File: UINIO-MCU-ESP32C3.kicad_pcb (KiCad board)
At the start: 2 copper layers, 60.3 x 20.4 mm, 50 parts, among them J1 Conn_01x15_Male, J2 外接串行下载接口, J3 Conn_01x15_Male, SW1 复位按键, SW2 下载按键, U1 ME6211C33M5G-N, U2 W25Q128JVSSIQ, U3 ESP32-C3, U4 CH343P, Y1 40MHz

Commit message: Complete wiring.
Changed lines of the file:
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@@
   (segment (start 134.37 111.72) (end 138.18 111.72) (width 0.5) (layer "B.Cu") (net 4))
   (segment (start 129.62 100.52) (end 129.62 106.97) (width 0.5) (layer "B.Cu") (net 4))
-  (segment (start 167.73 101.035903) (end 167.73 99.95) (width 0.2) (layer "F.Cu") (net 5))
   (segment (start 170.155 98.43) (end 169.25 98.43) (width 0.2) (layer "F.Cu") (net 5))
+  (segment (start 168.083553 99.596446) (end 169.25 98.43) (width 0.2) (layer "F.Cu") (net 5))
+  (segment (start 167.73 100.45) (end 167.73 101.035903) (width 0.2) (layer "F.Cu") (net 5))
   (segment (start 166.300677 102.465226) (end 167.73 101.035903) (width 0.2) (layer "F.Cu") (net 5))
-  (segment (start 167.73 99.95) (end 169.25 98.43) (width 0.2) (layer "F.Cu") (net 5))
+  (arc (start 167.73 100.45) (mid 167.821884 99.988059) (end 168.083552 99.596445) (width 0.2) (layer "F.Cu") (net 5))
   (segment (start 164.43 98.45) (end 164.43 100.093263) (width 0.2) (layer "F.Cu") (net 6))
   (segment (start 153.185 104.575) (end 150.51 104.575) (width 0.2) (layer "F.Cu") (net 6))
@@
   (via (at 131.62 96.7605) (size 0.5) (drill 0.2) (layers "F.Cu" "B.Cu") (net 23))
   (via (at 131.63 101.73) (size 0.5) (drill 0.2) (layers "F.Cu" "B.Cu") (net 23))
+  (segment (start 165.095185 105.824815) (end 164.94 105.98) (width 0.2) (layer "B.Cu") (net 23))
+  (segment (start 131.63 97.6695) (end 131.62 97.6595) (width 0.2) (layer "B.Cu") (net 23))
+  (segment (start 161.82 105.98) (end 152.61 96.77) (width 0.2) (layer "B.Cu") (net 23))
+  (segment (start 164.94 105.98) (end 161.82 105.98) (width 0.2) (layer "B.Cu") (net 23))
+  (segment (start 131.62 96.77) (end 130.57 95.72) (width 0.2) (layer "B.Cu") (net 23))
   (segment (start 130.57 95.72) (end 130.57 94.15) (width 0.2) (layer "B.Cu") (net 23))
-  (segment (start 131.63 97.6695) (end 131.62 97.6595) (width 0.2) (layer "B.Cu") (net 23))
-  (segment (start 161.664815 105.824815) (end 152.61 96.77) (width 0.2) (layer "B.Cu") (net 23))
   (segment (start 131.63 101.73) (end 131.63 97.6695) (width 0.2) (layer "B.Cu") (net 23))
   (segment (start 152.61 96.77) (end 131.62 96.77) (width 0.2) (layer "B.Cu") (net 23))
-  (segment (start 131.62 96.77) (end 130.57 95.72) (width 0.2) (layer "B.Cu") (net 23))
-  (segment (start 165.095185 105.824815) (end 161.664815 105.824815) (width 0.2) (layer "B.Cu") (net 23))
   (segment (start 130.96 101.13) (end 134.259 101.13) (width 0.2) (layer "F.Cu") (net 24))
   (segment (start 165.804447 105.755553) (end 165.73303 105.755553) (width 0.2) (layer "F.Cu") (net 24))

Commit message: Ready for release.
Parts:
- AE1: value Antenna -> Antenna_Dipole
- moved C7 13.2 mm to (167.4, 98.5), turned to 90 degrees
- moved C5 12.9 mm to (166.5, 98.5), turned to 90 degrees
- moved C4 12.7 mm to (165.5, 98.5), turned to 90 degrees
- moved C19 2.41 mm to (156.5, 104.9)
- moved C18 1.63 mm to (156.4, 103.2)
- moved C8 1.53 mm to (169.0, 100.4), turned to -45 degrees
- moved C14 1.36 mm to (156.4, 98.6)
- moved R4 1.35 mm to (156.4, 99.7)
- moved C10 1.29 mm to (169.2, 102.8)
- moved L1 1.19 mm to (169.7, 99.1), turned to -135 degrees
- moved C6 1.14 mm to (171.0, 98.5), turned to -45 degrees
- moved C12 0.99 mm to (169.2, 103.7)
- moved R2 0.66 mm to (161.2, 98.5)
- moved AE1 0.46 mm to (175.5, 98.4)
- moved HOLE4 0.41 mm to (176.1, 111.7)
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- renumbered HOLE** to HOLE1, HOLE** to HOLE2, HOLE** to HOLE3, HOLE** to HOLE4, HOLE** to HOLE5
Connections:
- AE1 pad 1: Net-(AE1-Pad1) -> GND
- AE1 pad 2: (no net) -> Net-(AE1-Pad2)
- C6 pad 1: Net-(AE1-Pad1) -> Net-(AE1-Pad2)
- L1 pad 1: Net-(AE1-Pad1) -> Net-(AE1-Pad2)
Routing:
- net GND: track 143.0 -> 185.3 mm, vias 27 -> 24
- net Net-(AE1-Pad2): track 0.00 -> 6.24 mm
- net Net-(AE1-Pad1): track 4.82 -> 0.00 mm
- net /VDD_3.3V: track 132.1 -> 134.8 mm
- net Net-(C8-Pad1): track 6.10 -> 4.27 mm
- net /CHIP_EN: track 32.7 -> 31.9 mm
- net /GPIO5/ADC2/SCL: track 8.25 -> 9.00 mm
- net /VDD_SPI/GPIO11: track 22.7 -> 22.2 mm
- net /GPIO1/U1RXD: vias 0 -> 1
- net /GPIO0/U1TXD: vias 0 -> 1
- net /GPIO2: vias 0 -> 1
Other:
- board size 60.3 x 20.4 mm -> 59.8 x 20.4 mm
- board text added: "ADC2 IO5 SCL"
- board text added: "CHIP_EN"
- board text added: "IO0 TXD1"
- board text added: "IO1 RXD1"
- board text added: "IO11 VDD_SPI"
- board text added: "IO12 SPIHD"
- board text added: "IO13 SPIWP"
- board text added: "IO18 USB_D-"
- board text added: "IO19 USB_D+"
- board text added: "IO8"
- board text added: "IO8 PWM"
- board text added: "IO9 BOOT"

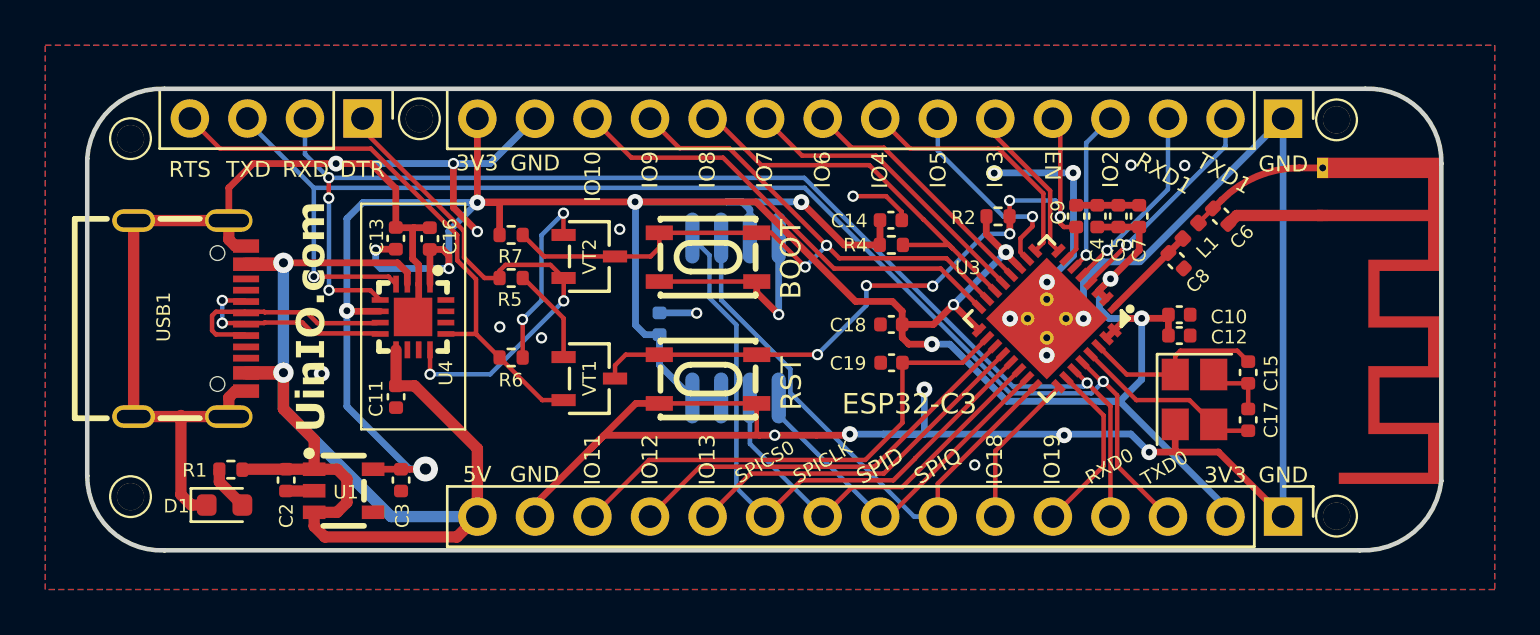
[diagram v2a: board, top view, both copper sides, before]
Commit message: Release UINIO-MCU-ESP32C3 version 1.0.0.
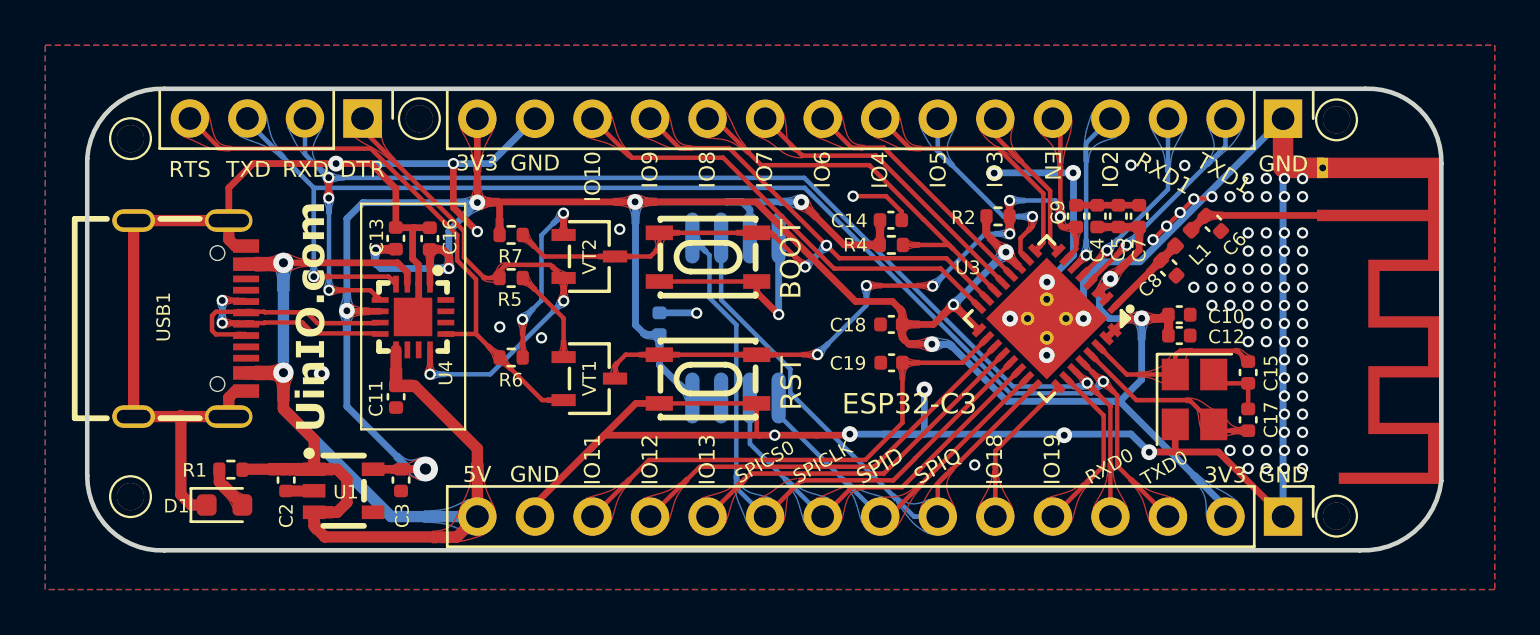
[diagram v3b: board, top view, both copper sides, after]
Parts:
- AE1: value Antenna_Dipole -> Antenna_Chip
- moved ? 1.36 mm to (164.3, 102.9)
- moved C6 0.46 mm to (170.7, 98.8)
- moved C8 0.46 mm to (168.7, 100.7)
- moved L1 0.46 mm to (169.3, 99.4)
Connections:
- AE1 pad 1: GND -> Net-(AE1-Pad1)
- AE1 pad 2: Net-(AE1-Pad2) -> GND
- C6 pad 1: Net-(AE1-Pad2) -> Net-(AE1-Pad1)
- L1 pad 1: Net-(AE1-Pad2) -> Net-(AE1-Pad1)
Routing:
- net Net-(AE1-Pad2): track 6.24 -> 0.00 mm
- net Net-(AE1-Pad1): track 0.00 -> 6.08 mm
- net GND: track 185.3 -> 190.0 mm, vias 24 -> 92
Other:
- board text added: "ADC1 IO4 SDA"

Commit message: Release UINIO-MCU-ESP32C3 version 1.0.0.
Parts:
- moved ? 0.49 mm to (164.8, 102.9)
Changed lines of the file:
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@@
   )
   (footprint "LOGO" (layer "B.Cu")
-    (at 164.311731 102.941526 180)
+    (at 164.8 102.941526 180)
     (attr board_only exclude_from_pos_files exclude_from_bom)
     (fp_text reference "" (at 0 0) (layer "B.SilkS")

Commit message: update
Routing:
- net GND: track 190.0 -> 210.5 mm, vias 92 -> 93

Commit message: Fix bug.
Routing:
- net GND: vias 93 -> 101

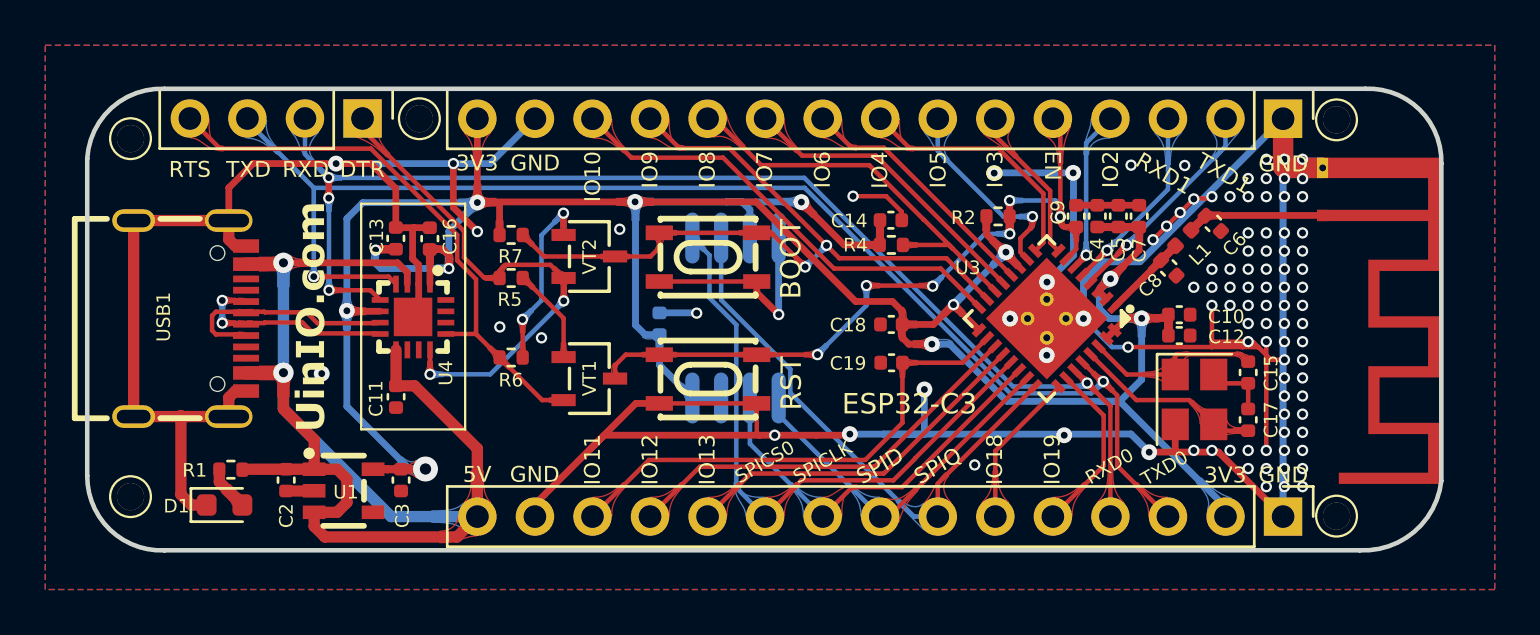
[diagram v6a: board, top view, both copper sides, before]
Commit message: Release UINIO-MCU-ESP32C3 2.0.0.
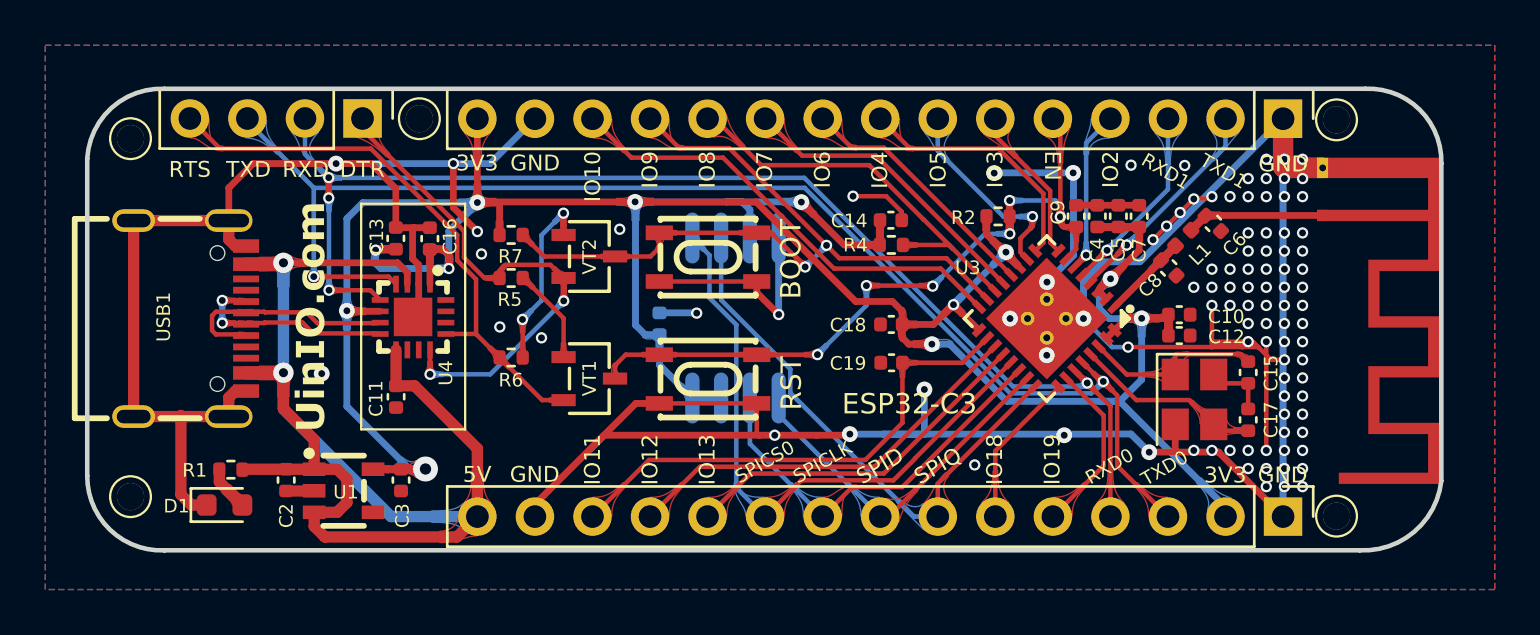
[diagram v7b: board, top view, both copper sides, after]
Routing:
- net GND: vias 101 -> 102
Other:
- board text added: "Version 2.0.0"
- board text removed: "Version 1.0.0"
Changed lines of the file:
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@@
     (effects (font (size 0.5 0.5) (thickness 0.1)) (justify left mirror))
   )
-  (gr_text "Version 1.0.0" (at 122.94 102.94 90) (layer "B.SilkS")
+  (gr_text "Version 2.0.0" (at 122.99 102.97 90) (layer "B.SilkS")
     (effects (font (size 0.7 0.7) (thickness 0.15)) (justify mirror))
   )
@@
     (effects (font (size 0.5 0.5) (thickness 0.1)) (justify right mirror))
   )
-  (gr_text "RXD1" (at 168.49 96.58 -30) (layer "F.SilkS")
-    (effects (font (size 0.7 0.7) (thickness 0.1)))
+  (gr_text "RXD1" (at 168.56 96.48 -30) (layer "F.SilkS")
+    (effects (font (size 0.6 0.6) (thickness 0.1)))
   )
   (gr_text "TXD" (at 128.08 96.4) (layer "F.SilkS")
@@
     (effects (font (size 0.6 0.6) (thickness 0.1)))
   )
-  (gr_text "TXD1" (at 171.13 96.58 -30) (layer "F.SilkS")
-    (effects (font (size 0.7 0.7) (thickness 0.1)))
+  (gr_text "TXD1" (at 171.11 96.48 -30) (layer "F.SilkS")
+    (effects (font (size 0.6 0.6) (thickness 0.1)))
   )
   (gr_text "IO3" (at 161.03 96.4 90) (layer "F.SilkS")
@@
     (effects (font (size 0.7 0.7) (thickness 0.1)))
   )
-  (gr_text "GND\n" (at 173.75 109.89) (layer "F.SilkS")
+  (gr_text "GND\n" (at 173.72 109.89) (layer "F.SilkS")
     (effects (font (size 0.7 0.7) (thickness 0.1)))
   )
@@
   (via (at 172.2 100.8) (size 0.5) (drill 0.3) (layers "F.Cu" "B.Cu") (free) (net 2))
   (via (at 169.8 108.8) (size 0.5) (drill 0.3) (layers "F.Cu" "B.Cu") (free) (net 2))
+  (via (at 138.36 100.13) (size 0.5) (drill 0.3) (layers "F.Cu" "B.Cu") (free) (net 2))
   (via (at 173 97.6) (size 0.5) (drill 0.3) (layers "F.Cu" "B.Cu") (free) (net 2))
   (via (at 172.2 108.8) (size 0.5) (drill 0.3) (layers "F.Cu" "B.Cu") (free) (net 2))

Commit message: Fix bug.
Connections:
- U4 pad 4: /U0TXD -> /U0RXD
- U4 pad 5: /U0RXD -> /U0TXD
